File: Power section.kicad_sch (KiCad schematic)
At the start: 9 parts, among them J2 USB3_A, U4 TLV76733, U5 USBLC6-2P6, U6 TPS7A0212

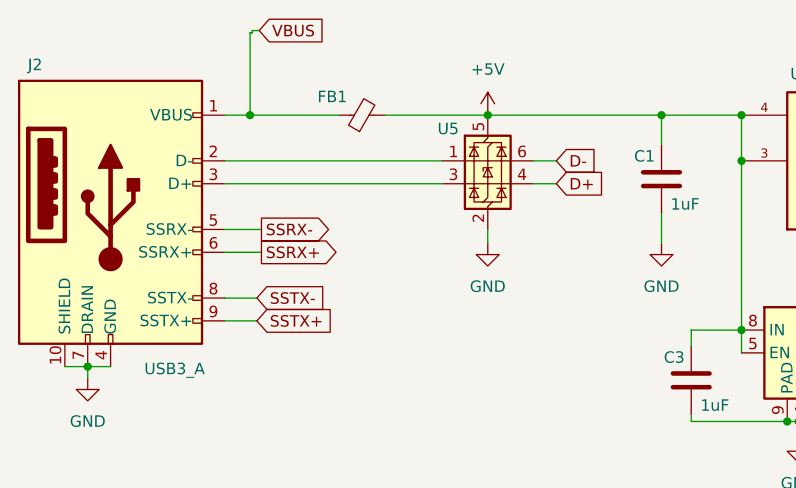
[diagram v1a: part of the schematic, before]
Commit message: usb connections done without 27 ohm, SMI connections done, EEPROM connections done.
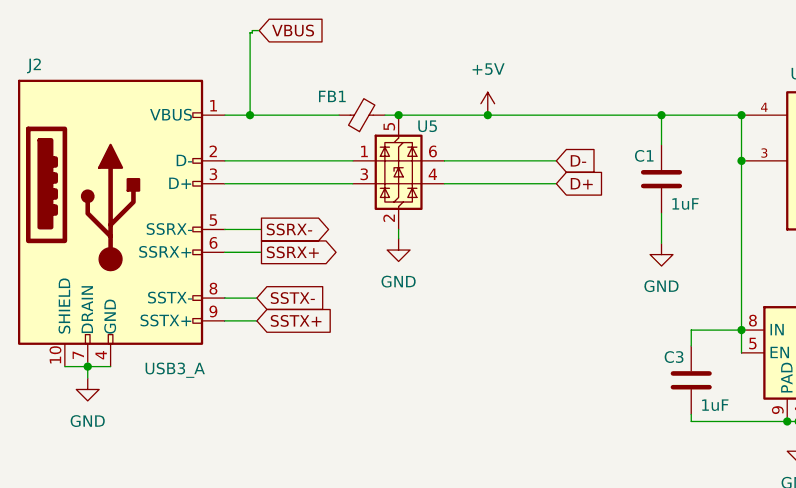
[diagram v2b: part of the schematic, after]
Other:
- moved on the sheet: U5
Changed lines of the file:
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@@
+	)
+	(junction
+		(at 76.2 38.1)
+		(diameter 0)
+		(color 0 0 0 0)
 	)
 	(junction
@@
 	(wire
 		(pts
-			(xy 86.106 52.324) (xy 86.106 50.8)
+			(xy 76.2 50.8) (xy 76.2 51.816)
 		)
 		(stroke
@@
 	(wire
 		(pts
-			(xy 93.726 45.72) (xy 91.186 45.72)
-		)
-		(stroke
-			(width 0)
-			(type default)
-		)
-	)
-	(wire
-		(pts
 			(xy 60.96 50.8) (xy 56.896 50.8)
 		)
@@
 	(wire
 		(pts
+			(xy 81.28 43.18) (xy 93.726 43.18)
+		)
+		(stroke
+			(width 0)
+			(type default)
+		)
+	)
+	(wire
+		(pts
 			(xy 119.38 72.136) (xy 120.65 72.136)
 		)
@@
 	(wire
 		(pts
-			(xy 56.896 45.72) (xy 81.026 45.72)
+			(xy 56.896 45.72) (xy 71.12 45.72)
 		)
 		(stroke
@@
 	(wire
 		(pts
-			(xy 74.676 38.1) (xy 86.106 38.1)
+			(xy 81.28 45.72) (xy 93.726 45.72)
+		)
+		(stroke
+			(width 0)
+			(type default)
+		)
+	)
+	(wire
+		(pts
+			(xy 74.676 38.1) (xy 76.2 38.1)
 		)
 		(stroke
@@
 	(wire
 		(pts
-			(xy 93.726 43.18) (xy 91.186 43.18)
-		)
-		(stroke
-			(width 0)
-			(type default)
-		)
-	)
-	(wire
-		(pts
 			(xy 159.766 48.26) (xy 149.86 48.26)
 		)
@@
 	(wire
 		(pts
-			(xy 56.896 43.18) (xy 81.026 43.18)
+			(xy 56.896 43.18) (xy 71.12 43.18)
 		)
 		(stroke
@@
 		(pts
 			(xy 56.896 38.1) (xy 59.69 38.1)
+		)
+		(stroke
+			(width 0)
+			(type default)
+		)
+	)
+	(wire
+		(pts
+			(xy 76.2 38.1) (xy 86.106 38.1)
 		)
 		(stroke
@@
 	(symbol
 		(lib_id "power:GND")
-		(at 86.106 52.324 0)
+		(at 76.2 51.816 0)
 		(unit 1)
 		(exclude_from_sim no)
@@
 		(fields_autoplaced yes)
 		(property "Reference" "#PWR02"
-			(at 86.106 58.674 0)
+			(at 76.2 58.166 0)
 			(effects
 				(font
@@
 		)
 		(property "Value" "GND"
-			(at 86.106 57.15 0)
+			(at 76.2 56.642 0)
 			(effects
 				(font
@@
 		)
 		(property "Footprint" ""
-			(at 86.106 52.324 0)
+			(at 76.2 51.816 0)
 			(effects
 				(font
@@
 		)
 		(property "Datasheet" ""
-			(at 86.106 52.324 0)
+			(at 76.2 51.816 0)
 			(effects
 				(font
@@
 		)
 		(property "Description" "Power symbol creates a global label with name \"GND\" , ground"
-			(at 86.106 52.324 0)
+			(at 76.2 51.816 0)
 			(effects
 				(font
@@
 	(symbol
 		(lib_id "Power_Protection:USBLC6-2P6")
-		(at 86.106 43.18 0)
+		(at 76.2 43.18 0)
 		(unit 1)
 		(exclude_from_sim no)
@@
 		(dnp no)
 		(property "Reference" "U5"
-			(at 80.518 39.624 0)
+			(at 78.232 39.37 0)
 			(effects
 				(font
@@
 		)
 		(property "Value" "USBLC6-2P6"
-			(at 88.138 50.292 0)
+			(at 78.232 50.292 0)
 			(effects
 				(font
@@
 		)
 		(property "Footprint" "Package_TO_SOT_SMD:SOT-666"
-			(at 87.122 49.911 0)
+			(at 77.216 49.911 0)
 			(effects
 				(font
@@
 		)
 		(property "Datasheet" "https://www.st.com/resource/en/datasheet/usblc6-2.pdf"
-			(at 87.122 51.816 0)
+			(at 77.216 51.816 0)
 			(effects
 				(font
@@
 		)
 		(property "Description" "Very low capacitance ESD protection diode, 2 data-line, SOT-666"
-			(at 86.106 43.18 0)
-			(effects
-				(font
+			(at 76.2 43.18 0)
+			(effects
+				(font

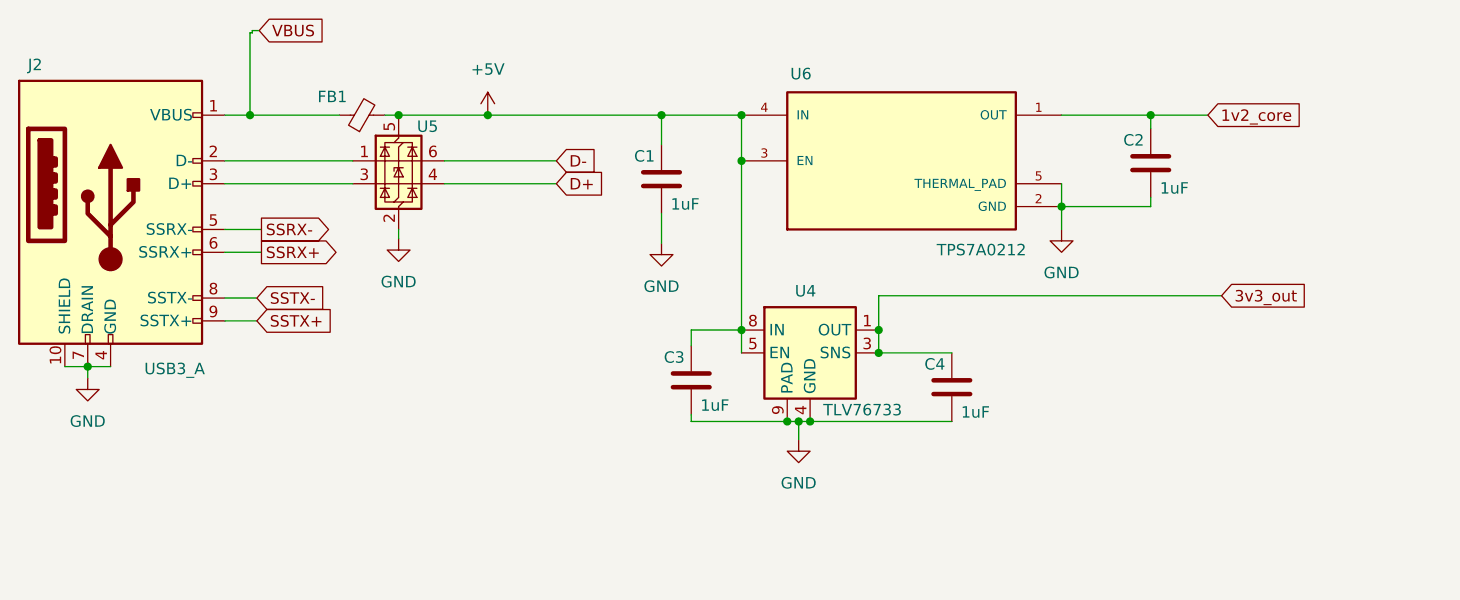
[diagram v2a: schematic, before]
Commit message: RGMII connections made, Clk circuitry made, 27 ohm resistors added
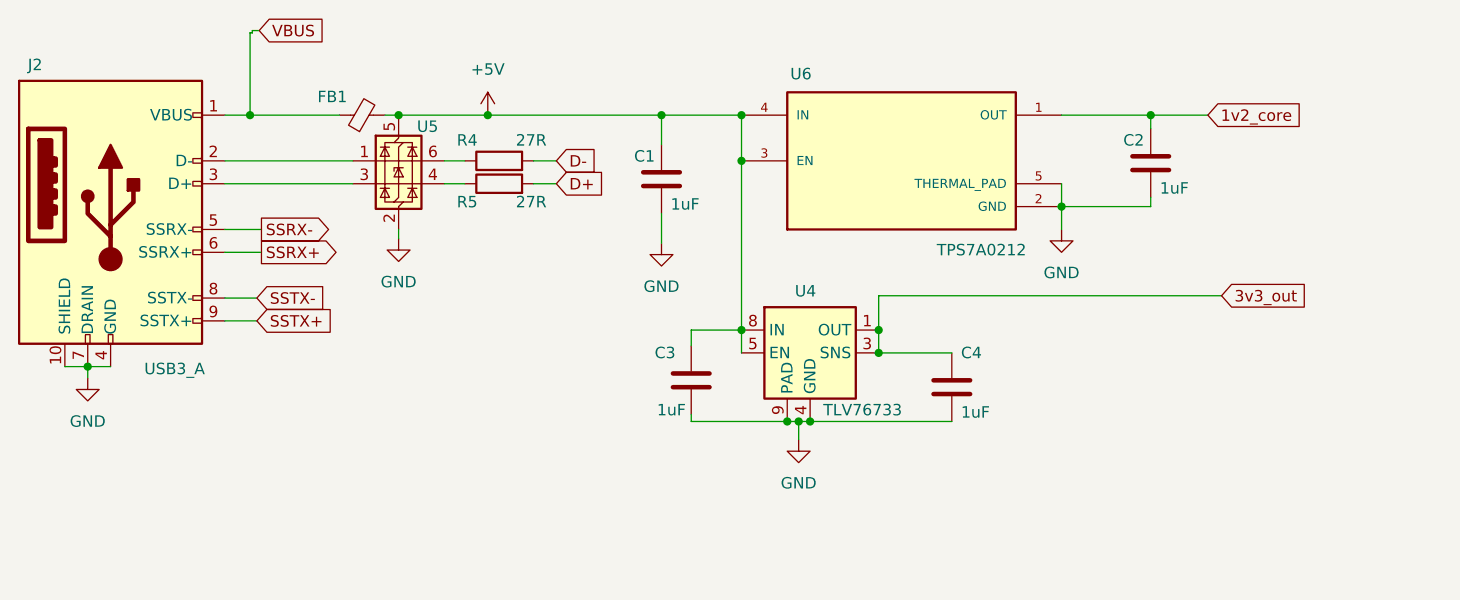
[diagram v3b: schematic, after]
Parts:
- added R4, R5: 27R, Resistor_SMD:R_1206, symbol Device:R
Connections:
- net D+: now also R5.2; no longer U5.4 (I/O2)
- net D-: now also R4.2; no longer U5.6 (I/O1)
- new net: R4.1, U5.6 (I/O1)
- new net: R5.1, U5.4 (I/O2)
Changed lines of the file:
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@@
+	(wire
+		(pts
+			(xy 81.28 45.72) (xy 83.566 45.72)
+		)
+		(stroke
+			(width 0)
+			(type default)
+		)
+	)
 	(wire
 		(pts
@@
 	(wire
 		(pts
-			(xy 81.28 43.18) (xy 93.726 43.18)
-		)
-		(stroke
-			(width 0)
-			(type default)
-		)
-	)
-	(wire
-		(pts
 			(xy 119.38 72.136) (xy 120.65 72.136)
 		)
@@
 	(wire
 		(pts
+			(xy 83.566 43.18) (xy 81.28 43.18)
+		)
+		(stroke
+			(width 0)
+			(type default)
+		)
+	)
+	(wire
+		(pts
 			(xy 159.766 47.244) (xy 159.766 48.26)
 		)
@@
 	(wire
 		(pts
-			(xy 81.28 45.72) (xy 93.726 45.72)
-		)
-		(stroke
-			(width 0)
-			(type default)
-		)
-	)
-	(wire
-		(pts
 			(xy 74.676 38.1) (xy 76.2 38.1)
 		)
@@
 	(wire
 		(pts
+			(xy 91.186 45.72) (xy 93.726 45.72)
+		)
+		(stroke
+			(width 0)
+			(type default)
+		)
+	)
+	(wire
+		(pts
 			(xy 167.64 58.166) (xy 129.54 58.166)
 		)
@@
 		(pts
 			(xy 56.896 43.18) (xy 71.12 43.18)
+		)
+		(stroke
+			(width 0)
+			(type default)
+		)
+	)
+	(wire
+		(pts
+			(xy 91.186 43.18) (xy 93.726 43.18)
 		)
 		(stroke
@@
 		(dnp no)
 		(property "Reference" "C4"
-			(at 134.62 65.786 0)
+			(at 138.684 64.516 0)
 			(effects
 				(font
@@
 				(path "/b00c1253-ab18-4b3e-8546-134ebc6e3f42/f3eed1fe-b26b-43be-93b7-52b7c59d4eab"
 					(reference "C4")
+					(unit 1)
+				)
+			)
+		)
+	)
+	(symbol
+		(lib_id "Device:R")
+		(at 87.376 43.18 90)
+		(unit 1)
+		(exclude_from_sim no)
+		(in_bom yes)
+		(on_board yes)
+		(dnp no)
+		(property "Reference" "R4"
+			(at 83.82 40.894 90)
+			(effects
+				(font
+					(size 1.27 1.27)
+				)
+			)
+		)
+		(property "Value" "27R"
+			(at 90.932 40.894 90)
+			(effects
+				(font
+					(size 1.27 1.27)
+				)
+			)
+		)
+		(property "Footprint" "Resistor_SMD:R_1206"
+			(at 87.376 44.958 90)
+			(effects
+				(font
+					(size 1.27 1.27)
+				)
+				(hide yes)
+			)
+		)
+		(property "Datasheet" "~"
+			(at 87.376 43.18 0)
+			(effects
+				(font
+					(size 1.27 1.27)
+				)
+				(hide yes)
+			)
+		)
+		(property "Description" "Resistor"
+			(at 87.376 43.18 0)
+			(effects
+				(font
+					(size 1.27 1.27)
+				)
+				(hide yes)
+			)
+		)
+		(pin "2"
+		)
+		(pin "1"
+		)
+		(instances
+			(project ""
+				(path "/b00c1253-ab18-4b3e-8546-134ebc6e3f42/f3eed1fe-b26b-43be-93b7-52b7c59d4eab"
+					(reference "R4")
 					(unit 1)
 				)
@@
 		(dnp no)
 		(property "Reference" "C3"
-			(at 105.664 65.024 0)
+			(at 104.648 64.516 0)
 			(effects
 				(font
@@
 		)
 		(property "Value" "1uF"
-			(at 109.728 70.358 0)
+			(at 104.902 70.866 0)
 			(effects
 				(font
@@
 					(unit 1)
 				)
+			)
+		)
+	)
+	(symbol
+		(lib_id "Device:R")
+		(at 87.376 45.72 90)
+		(unit 1)
+		(exclude_from_sim no)
+		(in_bom yes)
+		(on_board yes)
+		(dnp no)
+		(property "Reference" "R5"
+			(at 83.82 47.752 90)
+			(effects
+				(font
+					(size 1.27 1.27)
+				)
+			)
+		)
+		(property "Value" "27R"
+			(at 90.932 47.752 90)
+			(effects
+				(font
+					(size 1.27 1.27)
+				)
+			)
+		)
+		(property "Footprint" "Resistor_SMD:R_1206"
+			(at 87.376 47.498 90)
+			(effects
+				(font
+					(size 1.27 1.27)
+				)
+				(hide yes)
+			)
+		)
+		(property "Datasheet" "~"
+			(at 87.376 45.72 0)
+			(effects
+				(font
+					(size 1.27 1.27)
+				)
+				(hide yes)
+			)
+		)
+		(property "Description" "Resistor"
+			(at 87.376 45.72 0)
+			(effects
+				(font
+					(size 1.27 1.27)
+				)
+				(hide yes)
+			)
+		)
+		(pin "2"
+		)
+		(pin "1"
+		)
+		(instances
+			(project "USB_3.1_to_Ethernet"
+				(path "/b00c1253-ab18-4b3e-8546-134ebc6e3f42/f3eed1fe-b26b-43be-93b7-52b7c59d4eab"
+					(reference "R5")
+					(unit 1)
+				)

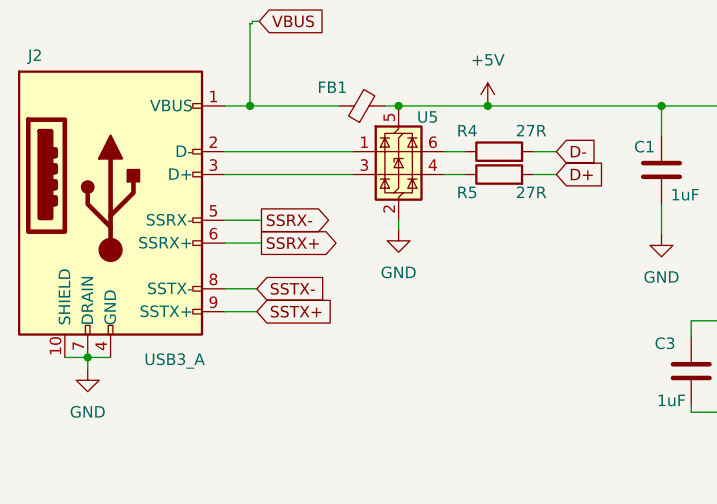
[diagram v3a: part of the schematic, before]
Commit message: Added 27R resistors to RGMII interface, added 0.1uF AC coupling caps on sstx/rx, Magjack connections done
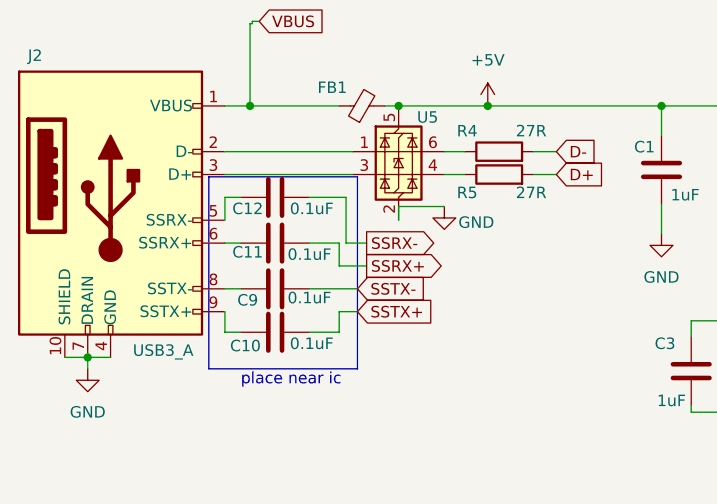
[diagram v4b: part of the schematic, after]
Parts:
- added C10, C11, C12, C9: 0.1uF, Capacitor_SMD:C_1206_3216Metric_Pad1.33x1.80mm_HandSolder, symbol Device:C
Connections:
- net SSRX+: now also C11.2; no longer J2.6 (SSRX+)
- net SSRX-: now also C12.2; no longer J2.5 (SSRX-)
- net SSTX+: now also C10.2; no longer J2.9 (SSTX+)
- net SSTX-: now also C9.2; no longer J2.8 (SSTX-)
- new net: C9.1, J2.8 (SSTX-)
- new net: C12.1, J2.5 (SSRX-)
- new net: C11.1, J2.6 (SSRX+)
- new net: C10.1, J2.9 (SSTX+)
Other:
- note added: "place near ic"

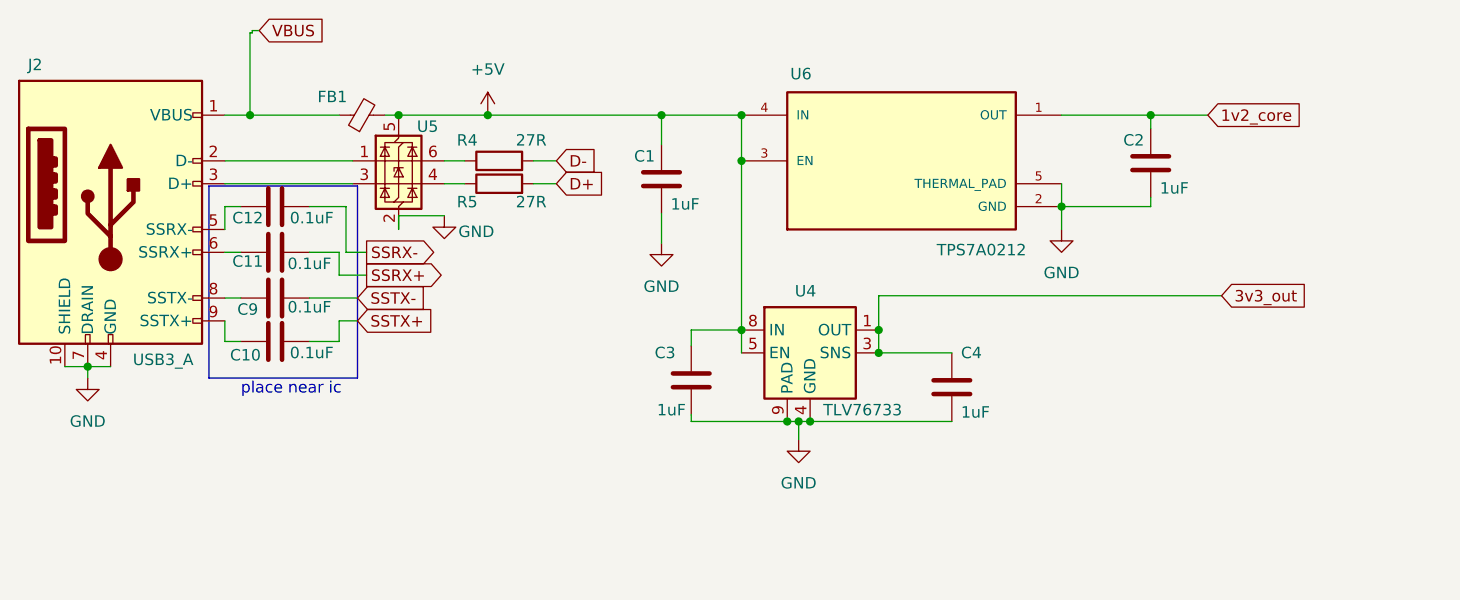
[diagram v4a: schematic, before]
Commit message: no major changes, APll tied to 3v3
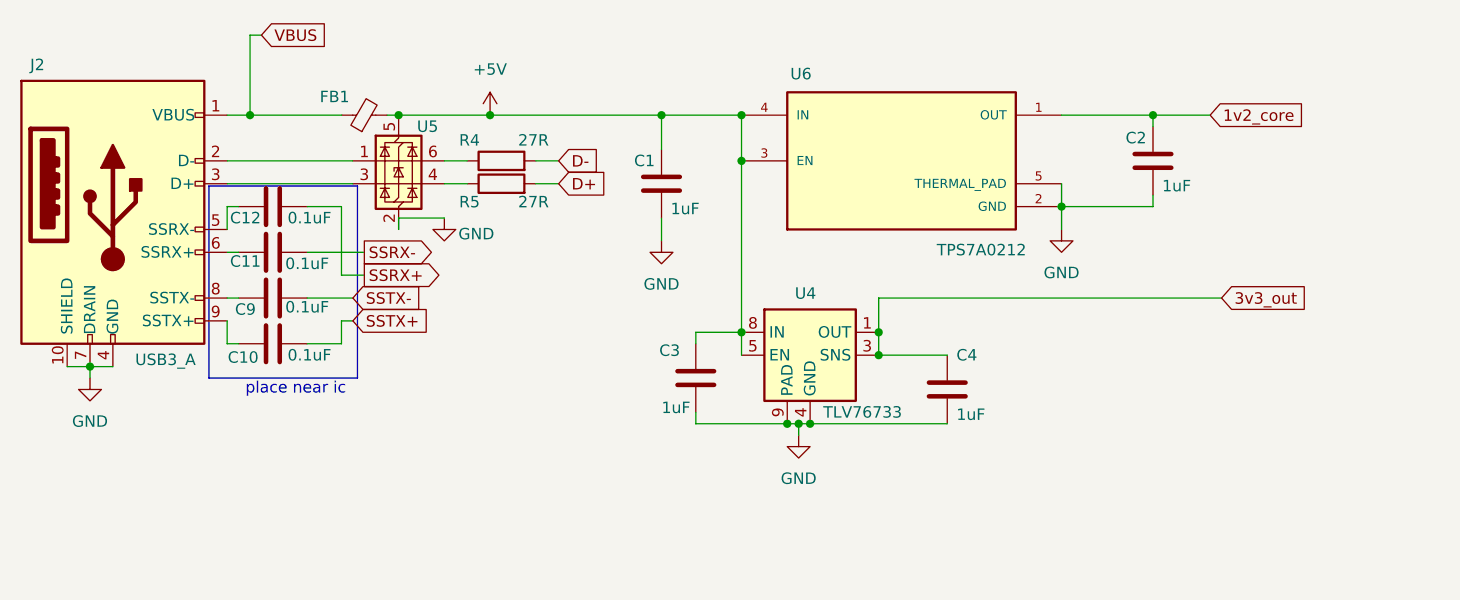
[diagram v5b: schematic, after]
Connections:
- net SSRX+: now also C12.2; no longer C11.2
- net SSRX-: now also C11.2; no longer C12.2
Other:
- moved on the sheet: C1, C3, C4

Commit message: 1. Decoupling capacitors for Lan7801 ic added 2. 3.3v Input given to TPS7A0212 instead of 5v 3. Ref+Rfilt resistor capacitor added 4. Iset resistor 12K added 5. Test Pull-down and Duplex Pull-up 10K added
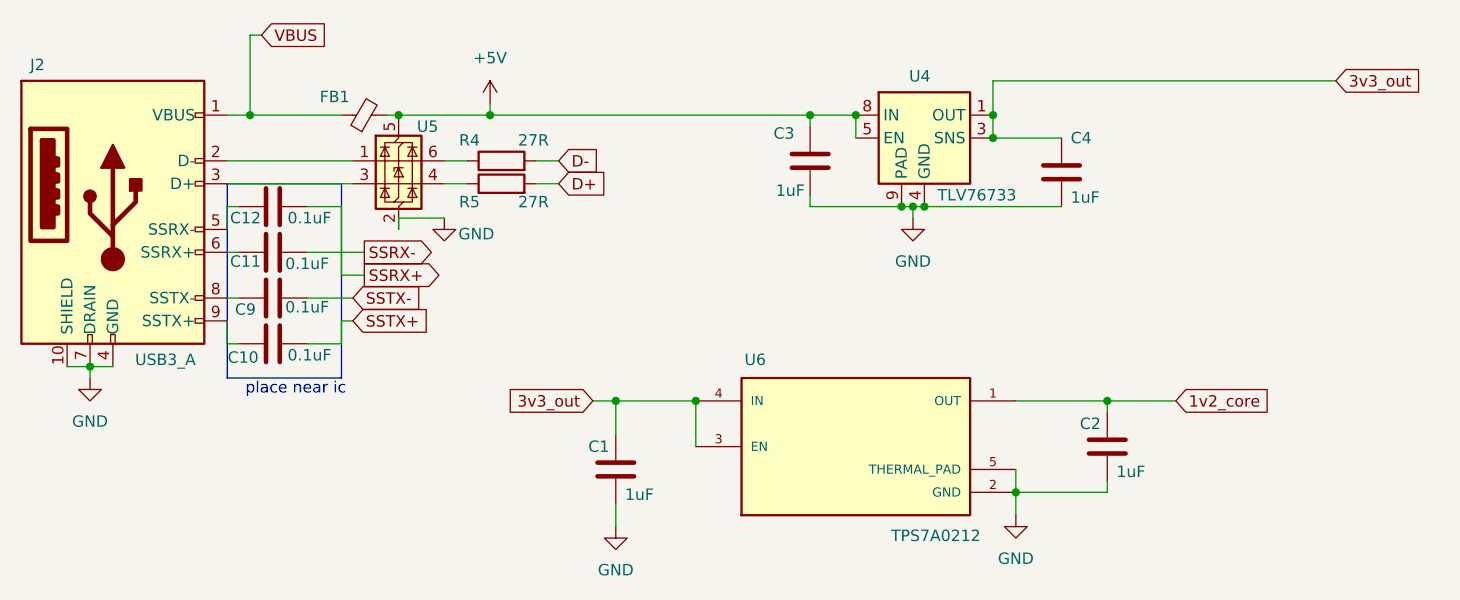
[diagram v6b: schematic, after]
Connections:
- net +5V: no longer C1.1, U6.3 (EN), U6.4 (IN)
- net 3v3_out: now also C1.1, U6.3 (EN), U6.4 (IN)
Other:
- moved on the sheet: C1, C2, C3, C4, U4, U6
